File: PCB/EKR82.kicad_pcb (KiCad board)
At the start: 2 copper layers, 173 x 137 mm, 99 parts, among them J1 LED, J2 4PIN, P1 i2c_pin, P2 i2c_pin, SW1 SW_PUSH, SW10 SW_PUSH, SW11 SW_PUSH, SW12 SW_PUSH, SW13 SW_PUSH, SW14 SW_PUSH, SW15 SW_PUSH, SW16 SW_PUSH, SW17 SW_PUSH, SW18 SW_PUSH, SW19 SW_PUSH, SW2 SW_PUSH, SW20 SW_PUSH, SW21 SW_PUSH, SW22 SW_PUSH, SW23 SW_PUSH, SW24 SW_PUSH, SW25 SW_PUSH, SW26 SW_PUSH, SW27 SW_PUSH, SW28 SW_PUSH, SW29 SW_PUSH, SW3 SW_PUSH, SW30 SW_PUSH, SW31 SW_PUSH, SW32 SW_PUSH, SW33 SW_PUSH, SW34 SW_PUSH, SW35 SW_PUSH, SW36 SW_PUSH, SW37 SW_PUSH, SW38 SW_PUSH, SW39 SW_PUSH, SW4 SW_PUSH, SW40 SW_PUSH, SW41 SW_PUSH, SW5 SW_PUSH, SW6 SW_PUSH, SW7 SW_PUSH, SW8 SW_PUSH, SW9 SW_PUSH, U1 ProMicro

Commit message: move SW41 and remove resistors
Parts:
- removed R1, R2: R, EKR82-footprint:RESISTOR_mini
- moved SW41 1.89 mm to (87.7, 137.0)
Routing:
- net SDA: track 27.5 -> 17.3 mm
- net SCL: track 24.2 -> 17.6 mm
- net VCC: track 70.4 -> 64.0 mm
- net col0: track 340.0 -> 344.5 mm
- net Net-(D41-Pad2): track 30.4 -> 30.1 mm, vias 0 -> 1
- net GND: vias 1134 -> 1128
- net (no net): vias 2 -> 6

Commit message: add backlight rgb WIP
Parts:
- added D42: SK6812MINI, LED_SMD:LED_SK6812MINI_PLCC4_3.5x3.5mm_P1.75mm, F.Cu at (80.4, 119.8)
- added D43: SK6812MINI, LED_SMD:LED_SK6812MINI_PLCC4_3.5x3.5mm_P1.75mm, F.Cu at (101.4, 140.7)
- added D44: SK6812MINI, LED_SMD:LED_SK6812MINI_PLCC4_3.5x3.5mm_P1.75mm, F.Cu at (125.8, 132.8)
- added D45: SK6812MINI, LED_SMD:LED_SK6812MINI_PLCC4_3.5x3.5mm_P1.75mm, F.Cu at (173.6, 132.4)
- added D46: SK6812MINI, LED_SMD:LED_SK6812MINI_PLCC4_3.5x3.5mm_P1.75mm, F.Cu at (206.4, 116.8)
- added D47: SK6812MINI, LED_SMD:LED_SK6812MINI_PLCC4_3.5x3.5mm_P1.75mm, F.Cu at (240.6, 117.0)
- added D48: SK6812MINI, LED_SMD:LED_SK6812MINI_PLCC4_3.5x3.5mm_P1.75mm, F.Cu at (241.2, 81.0)
- added D49: SK6812MINI, LED_SMD:LED_SK6812MINI_PLCC4_3.5x3.5mm_P1.75mm, F.Cu at (237.4, 23.6)
- added D50: SK6812MINI, LED_SMD:LED_SK6812MINI_PLCC4_3.5x3.5mm_P1.75mm, F.Cu at (192.4, 21.0)
- added D51: SK6812MINI, LED_SMD:LED_SK6812MINI_PLCC4_3.5x3.5mm_P1.75mm, F.Cu at (118.2, 20.8)
- added D52: SK6812MINI, LED_SMD:LED_SK6812MINI_PLCC4_3.5x3.5mm_P1.75mm, F.Cu at (87.0, 85.4)
- added D53: SK6812MINI, LED_SMD:LED_SK6812MINI_PLCC4_3.5x3.5mm_P1.75mm, B.Cu at (87.0, 85.4)
- added D54: SK6812MINI, LED_SMD:LED_SK6812MINI_PLCC4_3.5x3.5mm_P1.75mm, B.Cu at (80.4, 119.8)
- added D55: SK6812MINI, LED_SMD:LED_SK6812MINI_PLCC4_3.5x3.5mm_P1.75mm, B.Cu at (101.4, 140.8)
- added D56: SK6812MINI, LED_SMD:LED_SK6812MINI_PLCC4_3.5x3.5mm_P1.75mm, B.Cu at (125.8, 132.8)
- added D57: SK6812MINI, LED_SMD:LED_SK6812MINI_PLCC4_3.5x3.5mm_P1.75mm, B.Cu at (173.6, 132.4)
- added D58: SK6812MINI, LED_SMD:LED_SK6812MINI_PLCC4_3.5x3.5mm_P1.75mm, B.Cu at (206.4, 116.8)
- added D59: SK6812MINI, LED_SMD:LED_SK6812MINI_PLCC4_3.5x3.5mm_P1.75mm, B.Cu at (240.6, 117.0)
- added D60: SK6812MINI, LED_SMD:LED_SK6812MINI_PLCC4_3.5x3.5mm_P1.75mm, B.Cu at (241.2, 81.0)
- added D61: SK6812MINI, LED_SMD:LED_SK6812MINI_PLCC4_3.5x3.5mm_P1.75mm, B.Cu at (237.4, 23.6)
- added D62: SK6812MINI, LED_SMD:LED_SK6812MINI_PLCC4_3.5x3.5mm_P1.75mm, B.Cu at (192.4, 21.0)
- added D63: SK6812MINI, LED_SMD:LED_SK6812MINI_PLCC4_3.5x3.5mm_P1.75mm, B.Cu at (118.2, 20.8)
- added P3: led1, Connector_PinHeader_1.27mm:PinHeader_1x01_P1.27mm_Vertical, F.Cu at (87.8, 75.4)
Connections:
- J2 pad 3: Net-(J2-Pad3) -> DATA
- P2 pad 1: Net-(J2-Pad3) -> DATA
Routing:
- net VCC: track 64.0 -> 606.5 mm, vias 3 -> 14
- net Net-(D42-Pad3): track 0.00 -> 32.9 mm
- net Net-(D43-Pad1): track 0.00 -> 24.2 mm
- net Net-(D55-Pad1): track 0.00 -> 24.1 mm
- net Net-(D52-Pad3): track 0.00 -> 8.33 mm
- net Net-(D46-Pad1): vias 0 -> 1
- net GND: vias 1128 -> 1123
- net (no net): vias 6 -> 2

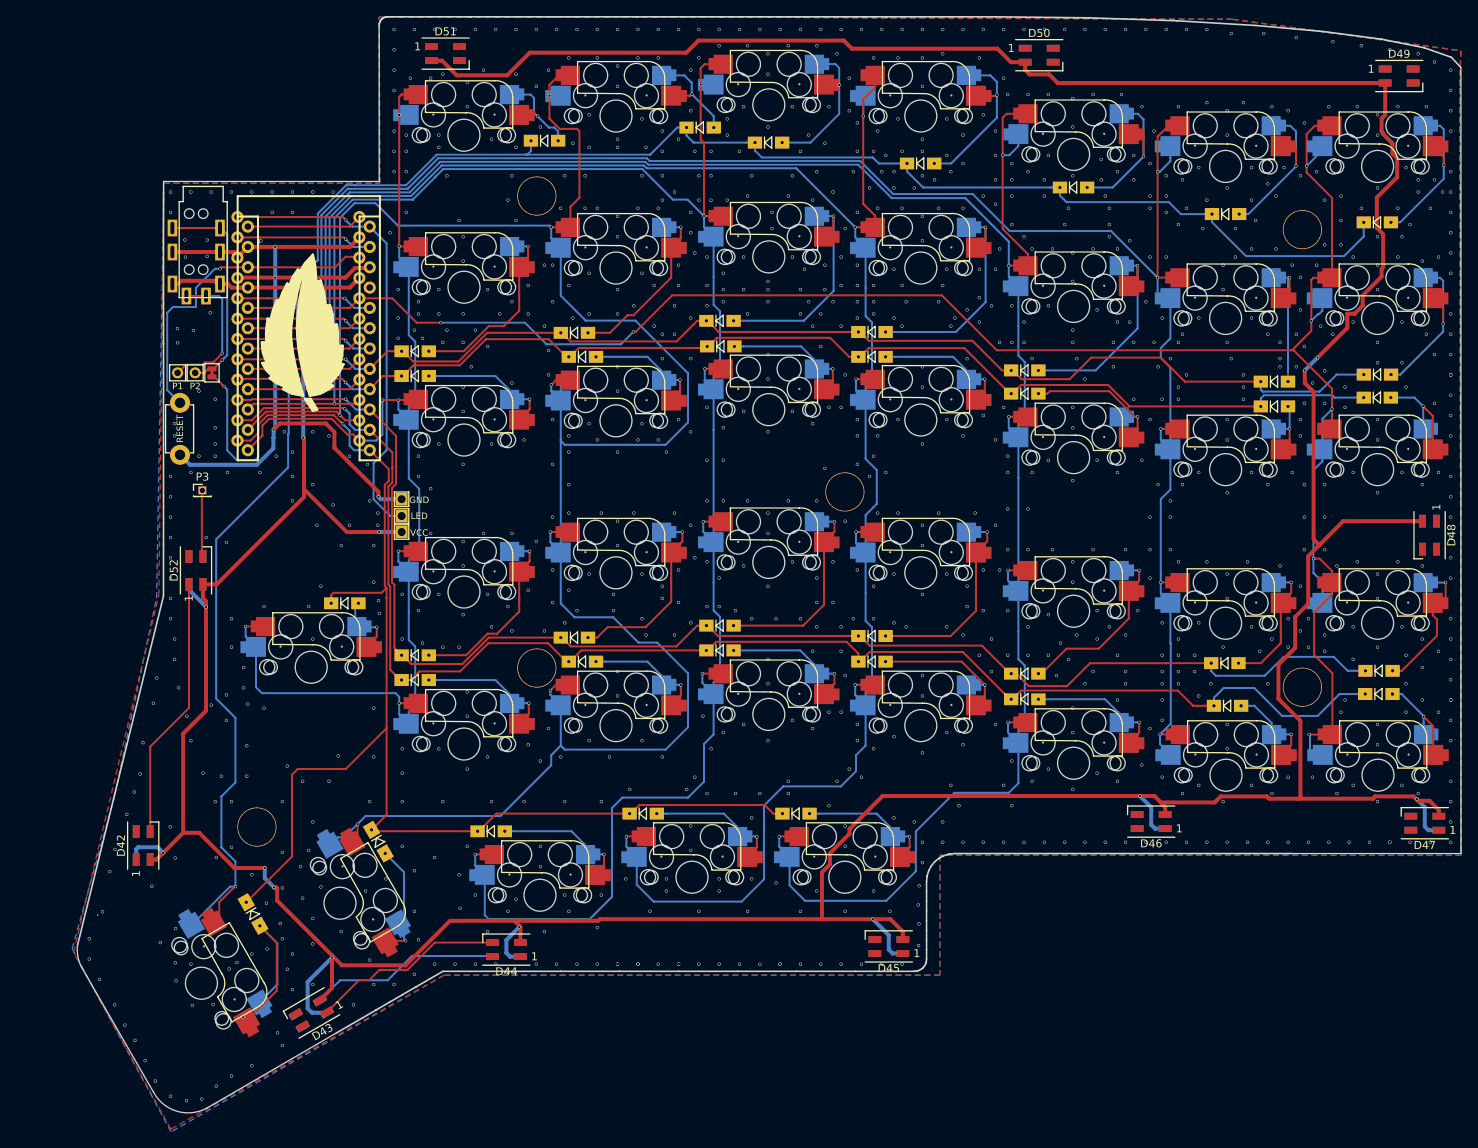
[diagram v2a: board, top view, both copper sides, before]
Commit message: add led and logo
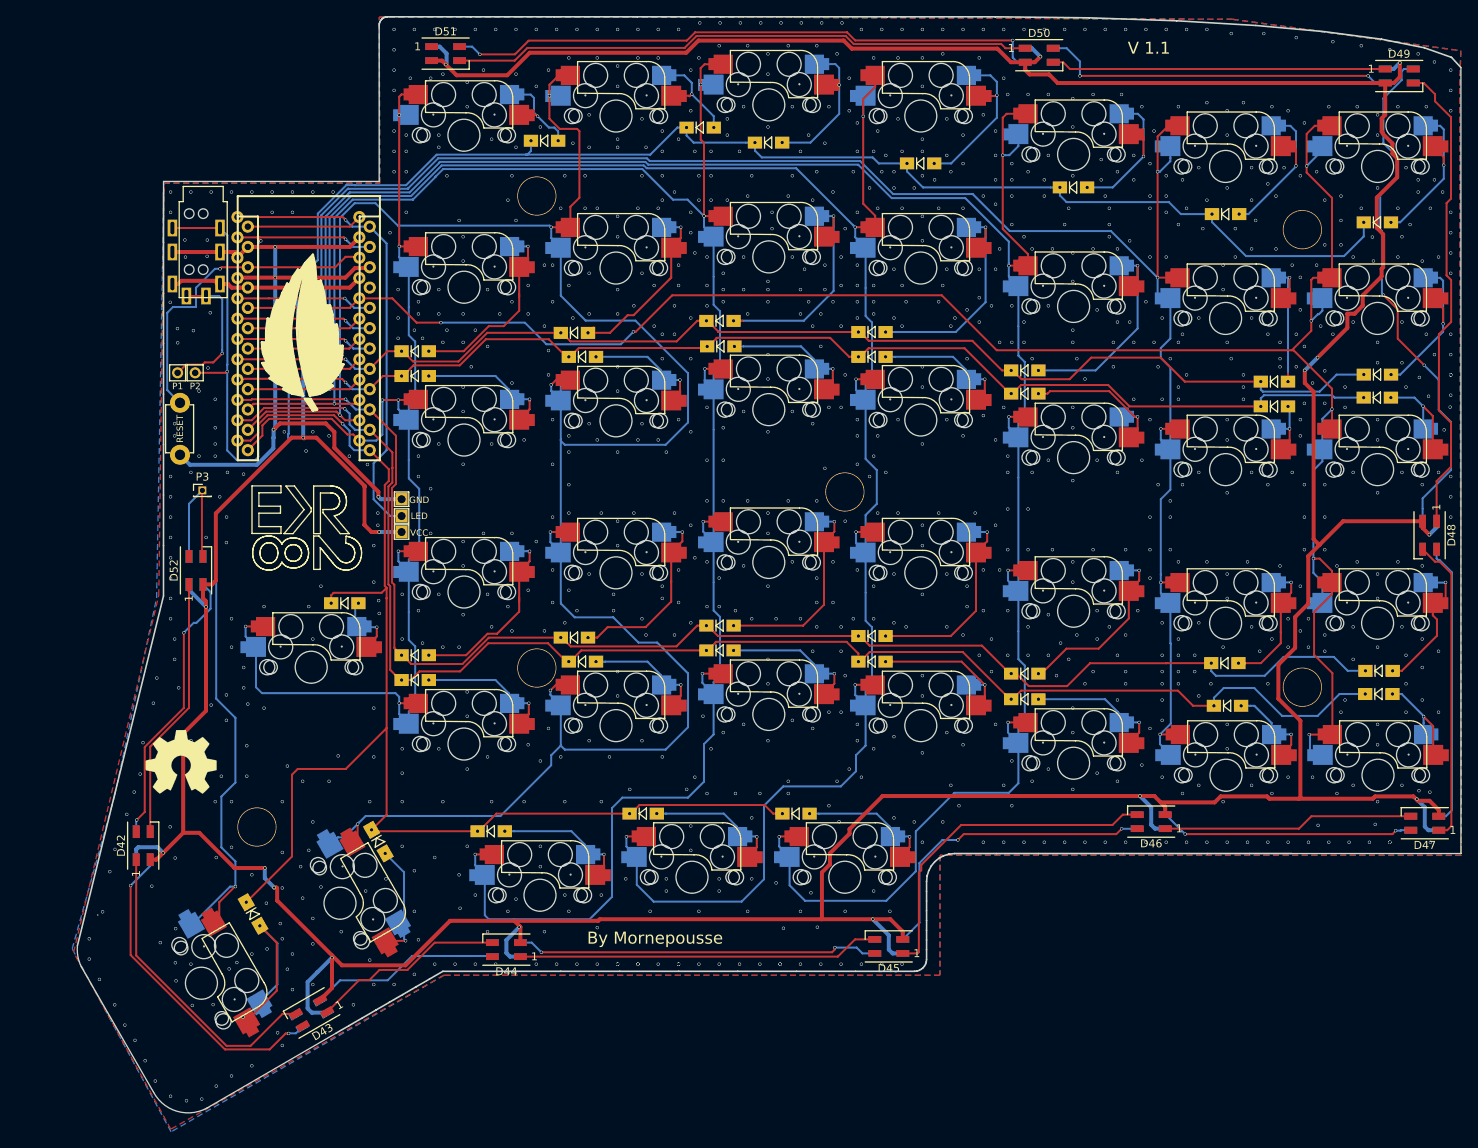
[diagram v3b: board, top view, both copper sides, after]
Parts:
- removed W1: jumper, EKR82-footprint:jumper_data
- added THLogo1: HOLE, EKR82-footprint:EKR82-2, B.Cu at (99.4, 73.0)
- added THLogo1: HOLE, EKR82-footprint:EKR82-2, F.Cu at (100.6, 72.6)
- added THLogo2: HOLE, Symbol:OSHW-Symbol_8.9x8mm_SilkScreen, F.Cu at (85.1, 109.3)
- added THLogo3: HOLE, Symbol:OSHW-Symbol_8.9x8mm_SilkScreen, B.Cu at (85.2, 109.4)
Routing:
- net Net-(D62-Pad1): track 0.00 -> 75.0 mm, vias 0 -> 2
- net Net-(D50-Pad1): track 0.00 -> 72.6 mm
- net Net-(D60-Pad1): track 0.00 -> 65.7 mm, vias 0 -> 2
- net Net-(D48-Pad1): track 0.00 -> 60.0 mm
- net Net-(D56-Pad1): track 0.00 -> 45.6 mm, vias 0 -> 2
- net Net-(D44-Pad1): track 0.00 -> 45.2 mm
- net Net-(D61-Pad1): track 0.00 -> 44.4 mm, vias 0 -> 2
- net Net-(D45-Pad1): track 0.00 -> 42.7 mm
- net Net-(D49-Pad1): track 0.00 -> 41.9 mm
- net Net-(D54-Pad1): track 0.00 -> 40.5 mm, vias 0 -> 2
- net Net-(D57-Pad1): track 0.00 -> 39.4 mm, vias 0 -> 2
- net Net-(D42-Pad1): track 0.00 -> 38.3 mm
- net Net-(D47-Pad1): track 0.00 -> 38.2 mm
- net Net-(D59-Pad1): track 0.00 -> 35.5 mm
- net Net-(D53-Pad1): track 0.00 -> 35.3 mm, vias 0 -> 2
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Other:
- board text added: "By Mornepousse"
- board text added: "V 1.1"

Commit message: Add top PCB and change diode footprint
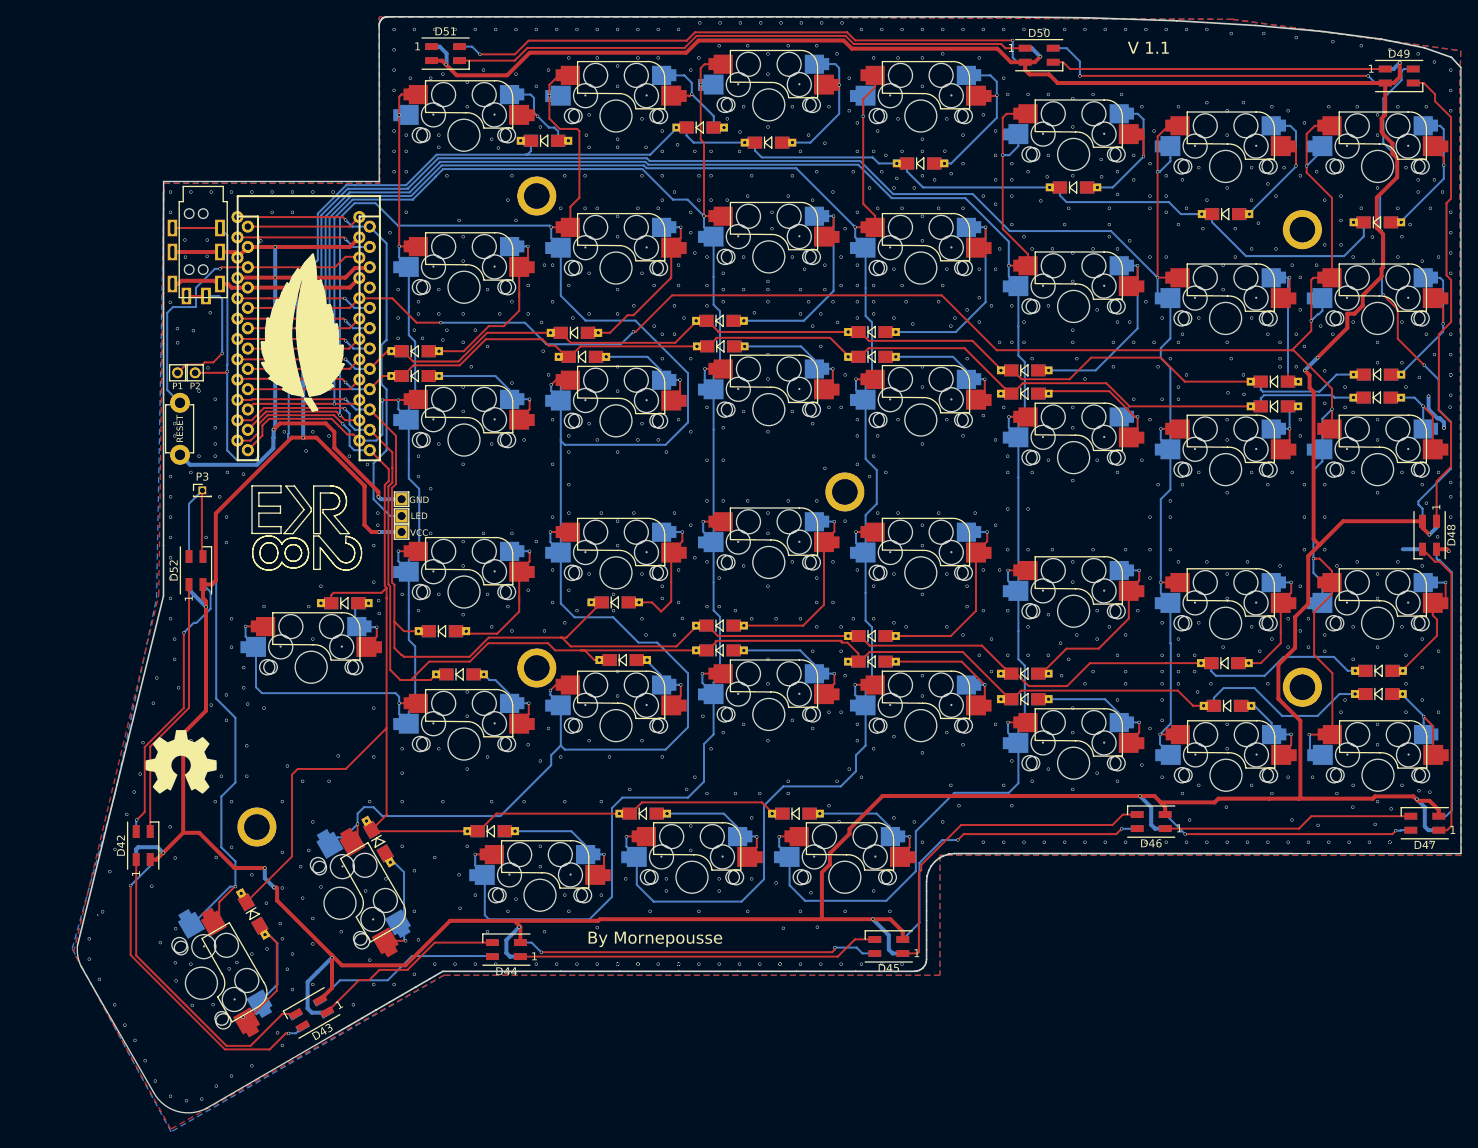
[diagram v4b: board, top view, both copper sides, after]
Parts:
- D1, D2, D25, D26, D27, D28, D29, D3, D30, D31, D32, D33, D34, D35, D36, D37, D38, D39, D4, D40, D41: footprint keyboard_switch:Diode_SOD123 -> EKR82-footprint:Diode_TH_SOD123EKR
- D10, D11, D12, D13, D14, D15, D16, D17, D18, D19, D20, D21, D22, D23, D24, D5, D6, D7, D8, D9: footprint EKR82-footprint:Diode_SOD123 -> EKR82-footprint:Diode_TH_SOD123EKR
- moved D14 6.74 mm to (139.4, 89.4)
- moved D19 5.64 mm to (120.0, 98.4)
- moved D20 5.10 mm to (140.4, 96.6)
- moved D13 4.53 mm to (117.8, 93.0)
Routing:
- net row2: track 181.0 -> 208.6 mm
- net row3: track 186.8 -> 211.4 mm
- net row1: track 152.5 -> 170.6 mm
- net row0: track 153.2 -> 171.3 mm
- net row5: track 179.5 -> 196.2 mm
- net row4: track 165.1 -> 181.1 mm
- net GND: track 102.0 -> 111.0 mm
- net Net-(D19-Pad2): track 19.1 -> 15.1 mm
- net Net-(D14-Pad2): track 26.0 -> 22.6 mm
- net Net-(D13-Pad2): track 26.7 -> 23.3 mm
- net Net-(D41-Pad2): track 30.1 -> 32.8 mm
- net Net-(D26-Pad2): track 16.9 -> 19.7 mm
- net Net-(D4-Pad2): track 31.0 -> 33.6 mm
- net Net-(D40-Pad2): track 22.4 -> 24.9 mm
- net Net-(D35-Pad2): track 21.1 -> 23.6 mm
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
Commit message: change arduino footprint and move
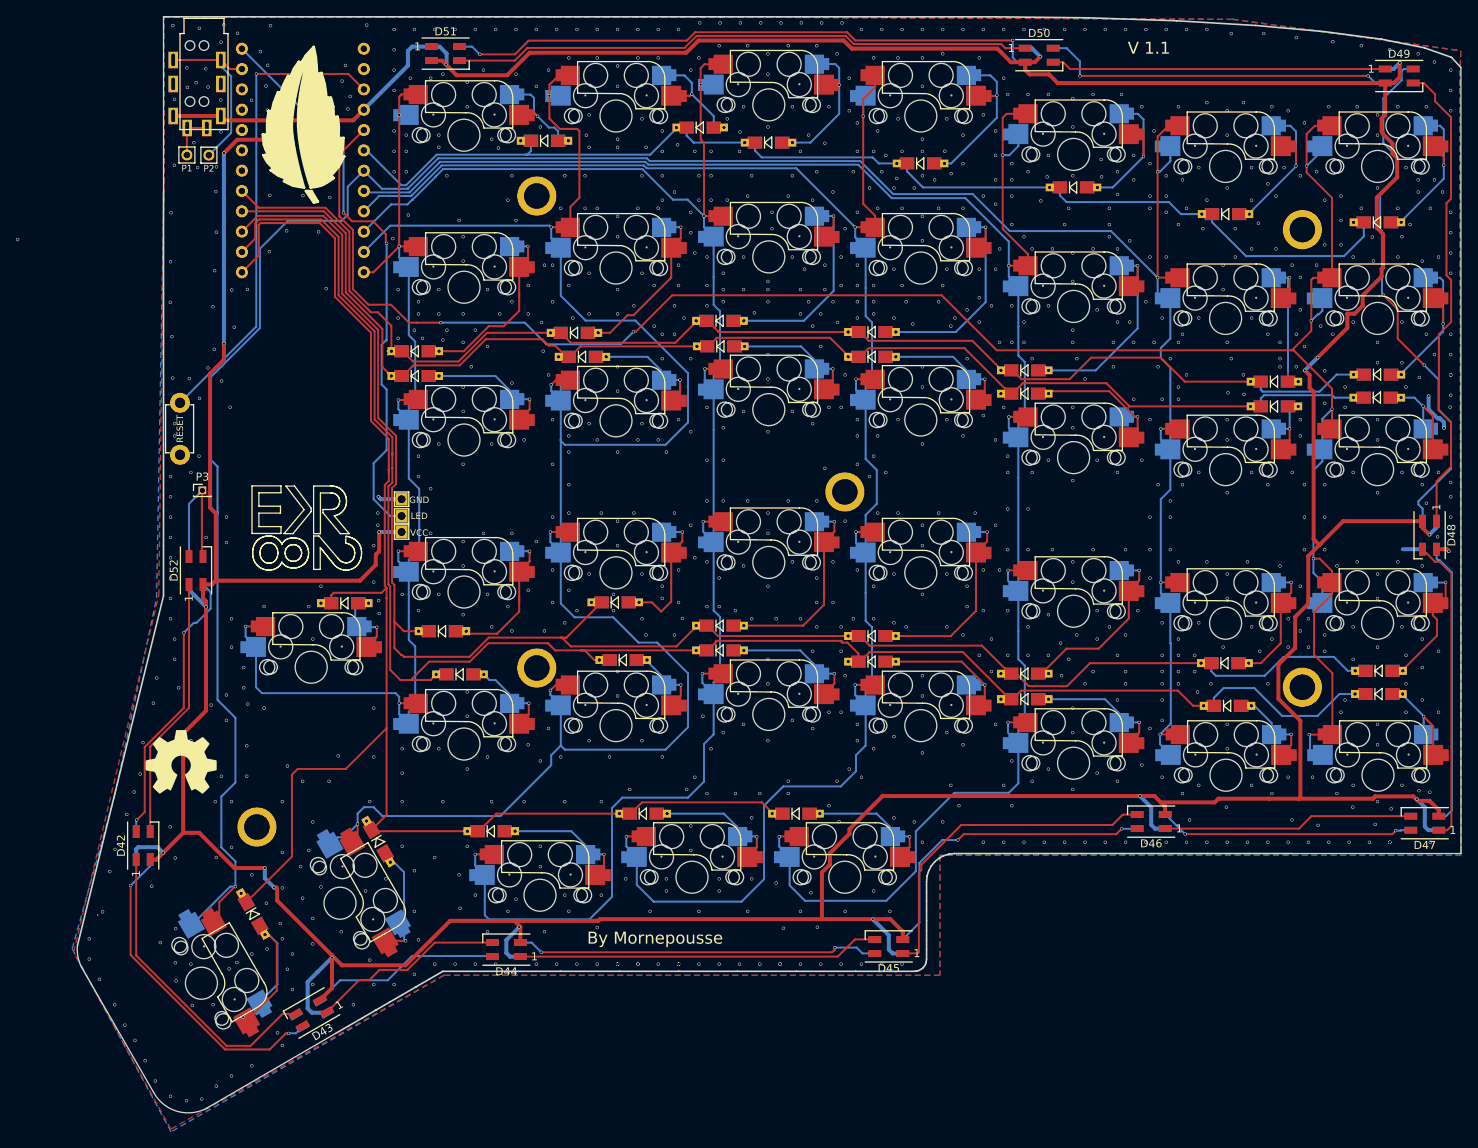
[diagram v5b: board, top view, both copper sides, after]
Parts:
- U1: footprint EKR82-footprint:ProMicro_rev2 -> EKR82-footprint:ProMicro_rev
- moved P2 27.3 mm to (88.6, 33.5)
- moved P1 27.3 mm to (85.9, 33.5)
- moved REF** 26.0 mm to (99.9, 30.0)
- moved REF** 26.0 mm to (99.5, 31.0)
- moved U1 21.8 mm to (100.4, 34.2)
- moved J2 21.0 mm to (88.0, 18.3)
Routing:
- net GND: track 111.0 -> 12.1 mm, vias 1093 -> 1117
- net DATA: track 87.8 -> 22.8 mm, vias 3 -> 0
- net col4: track 290.7 -> 247.4 mm, vias 7 -> 6
- net VCC: track 630.8 -> 673.1 mm
- net col3: track 264.6 -> 223.9 mm, vias 7 -> 6
- net col2: track 282.1 -> 241.8 mm, vias 7 -> 6
- net col1: track 299.6 -> 260.0 mm, vias 7 -> 6
- net row5: track 196.2 -> 160.9 mm, vias 1 -> 0
- net row4: track 181.1 -> 205.6 mm, vias 1 -> 0
- net row3: track 211.4 -> 234.0 mm, vias 1 -> 0
- net col5: track 169.7 -> 148.5 mm, vias 7 -> 6
- net row2: track 208.6 -> 229.1 mm, vias 1 -> 0
- net RESET: track 40.3 -> 59.3 mm
- net SCL: track 17.6 -> 0.00 mm, vias 1 -> 0
- net SDA: track 17.3 -> 0.00 mm, vias 1 -> 0
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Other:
- outline, holes or cut-outs redrawn

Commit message: little ajustements
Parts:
- RGB: renamed from P3; footprint Connector_PinHeader_1.27mm:PinHeader_1x01_P1.27mm_Vertical -> Connector_PinSocket_1.27mm:PinSocket_1x01_P1.27mm_Vertical
- moved D31 0.43 mm to (131.0, 31.8)
- moved RGB 0.21 mm to (87.6, 75.3)
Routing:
- net VCC: track 673.1 -> 691.6 mm
- net Net-(D14-Pad2): track 22.6 -> 18.5 mm
- net row2: track 229.1 -> 232.6 mm
- net col0: track 338.4 -> 341.3 mm
- net row4: track 205.6 -> 203.0 mm
- net col2: track 241.8 -> 244.3 mm
- net row0: track 184.9 -> 183.5 mm
- net Net-(D42-Pad3): track 32.9 -> 34.2 mm
- net Net-(D31-Pad2): track 15.2 -> 13.9 mm
- net col3: track 223.9 -> 225.2 mm
- net Net-(D53-Pad1): track 35.3 -> 36.6 mm
- net Net-(D17-Pad2): track 27.7 -> 27.0 mm
- net row5: track 160.9 -> 160.3 mm
- net GND: vias 1117 -> 1113
- net (no net): vias 6 -> 5
